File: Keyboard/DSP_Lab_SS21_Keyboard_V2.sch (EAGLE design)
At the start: 15 parts, among them J1 640455-2

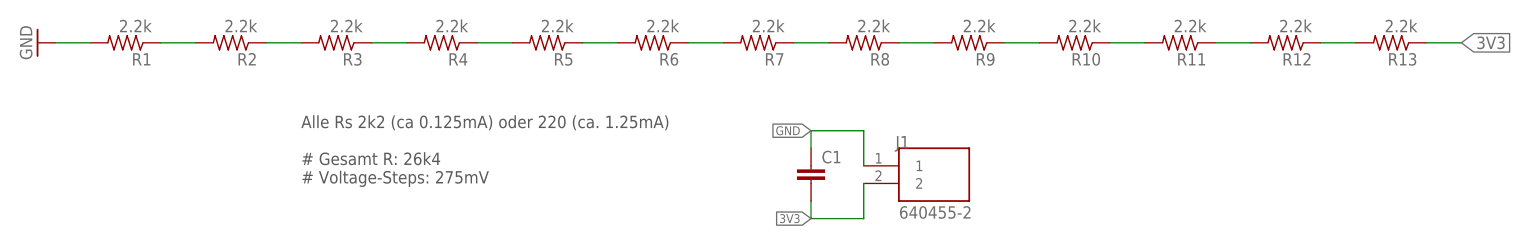
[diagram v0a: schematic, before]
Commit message: keyboard sch text edited
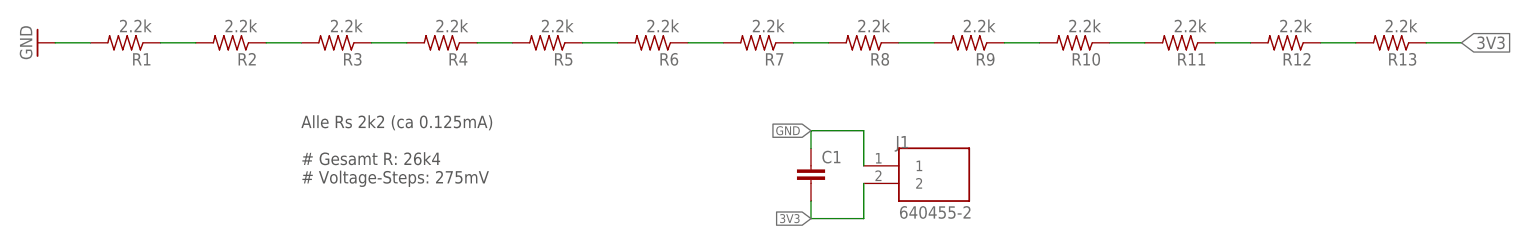
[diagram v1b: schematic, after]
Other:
- note added: "Alle Rs 2k2 (ca 0.125mA) # Gesamt R: 26k4 # Voltage-Steps: 275mV"
- note removed: "Alle Rs 2k2 (ca 0.125mA) oder 220 (ca. 1.25mA) # Gesamt R: 26k4 # Voltage-Steps: 275mV"
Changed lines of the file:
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@@
 <sheet>
 <plain>
-<text x="-55.88" y="0" size="1.778" layer="97">Alle Rs 2k2 (ca 0.125mA) oder 220 (ca. 1.25mA)
+<text x="-55.88" y="0" size="1.778" layer="97">Alle Rs 2k2 (ca 0.125mA)
 # Gesamt R: 26k4
 # Voltage-Steps: 275mV</text>

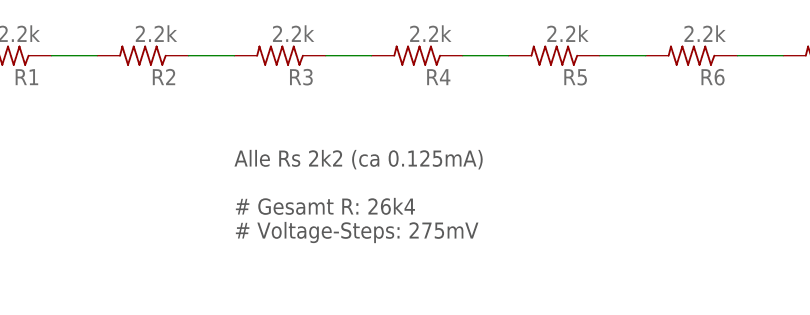
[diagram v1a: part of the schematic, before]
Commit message: Keyboard pictures added and sch updated
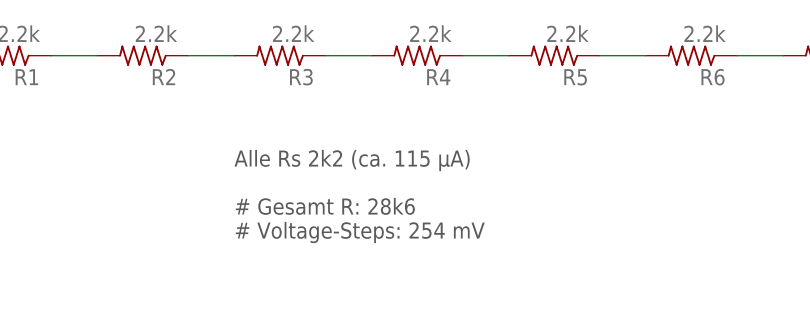
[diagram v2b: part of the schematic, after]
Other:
- note added: "Alle Rs 2k2 (ca. 115 µA) # Gesamt R: 28k6 # Voltage-Steps: 254 mV"
- note removed: "Alle Rs 2k2 (ca 0.125mA) # Gesamt R: 26k4 # Voltage-Steps: 275mV"
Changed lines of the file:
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@@
 <sheet>
 <plain>
-<text x="-55.88" y="0" size="1.778" layer="97">Alle Rs 2k2 (ca 0.125mA)
-# Gesamt R: 26k4
-# Voltage-Steps: 275mV</text>
+<text x="-55.88" y="0" size="1.778" layer="97">Alle Rs 2k2 (ca. 115 µA)
+# Gesamt R: 28k6
+# Voltage-Steps: 254 mV</text>
 </plain>
 <instances>
